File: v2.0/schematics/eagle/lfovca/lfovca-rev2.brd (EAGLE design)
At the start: 98.7 x 54.6 mm, 66 parts, among them IC1 TL082P, IC2 TL084P, T1 2N3904, T2 2N3904, T3 2N3904, T4 BC547, T5 BC547, T6 BC547

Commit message: LFOVCA: Optimize routes; cam outputs
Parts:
- moved R33 41.9 mm to (47.0, 39.4), turned to 270 degrees
- moved R13 38.1 mm to (69.8, 25.4), turned to 270 degrees
- moved R41 35.6 mm to (44.5, 12.7), turned to 0 degrees
- moved R39 25.5 mm to (31.8, 22.9), turned to 0 degrees
- moved R22 24.4 mm to (20.3, 11.4)
- moved R23 18.1 mm to (20.3, 15.2)
- moved R29 18.0 mm to (41.9, 22.9), turned to 0 degrees
- moved R34 17.8 mm to (49.5, 25.4)
- moved T2 14.2 mm to (5.08, 15.2)
- moved T3 14.2 mm to (11.4, 15.2)
- moved R8 12.6 mm to (81.3, 25.4), turned to 270 degrees
- moved R17 11.4 mm to (31.8, 11.4)
- moved R28 10.9 mm to (41.9, 26.7)
- moved R31 10.2 mm to (31.8, 26.7)
- moved R14 8.89 mm to (6.35, 24.1)
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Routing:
- net N$15: track 71.4 -> 13.8 mm, vias 2 -> 0
- net N$7: track 61.2 -> 25.8 mm, vias 1 -> 0
- net N$11: track 27.7 -> 9.05 mm
- net +12V: track 213.3 -> 198.5 mm, vias 0 -> 1
- net N$19: track 31.0 -> 16.5 mm
- net N$28: track 42.0 -> 27.9 mm, vias 1 -> 0
- net N$26: track 46.8 -> 32.8 mm
- net N$29: track 21.2 -> 7.93 mm
- net N$31: track 38.7 -> 51.8 mm, vias 1 -> 0
- net N$30: track 47.0 -> 58.7 mm
- net N$25: track 16.9 -> 7.34 mm
- net -12V: track 221.2 -> 230.2 mm, vias 1 -> 4
- net N$33: track 12.3 -> 20.6 mm
- net N$34: track 6.33 -> 14.4 mm
- net N$8: track 56.1 -> 50.0 mm, vias 1 -> 0
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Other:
- board text added: "ATTEN"
- board text added: "BIAS"
- board text added: "CV IN"
- board text added: "CV INIT"
- board text added: "LFO OUT"
- board text added: "LFOVCA rev2"
- board text added: "MIN LVL"
- board text added: "OFFSET"
- board text added: "RATE"
- board text added: "ROUND"
- board text added: "SYMM"

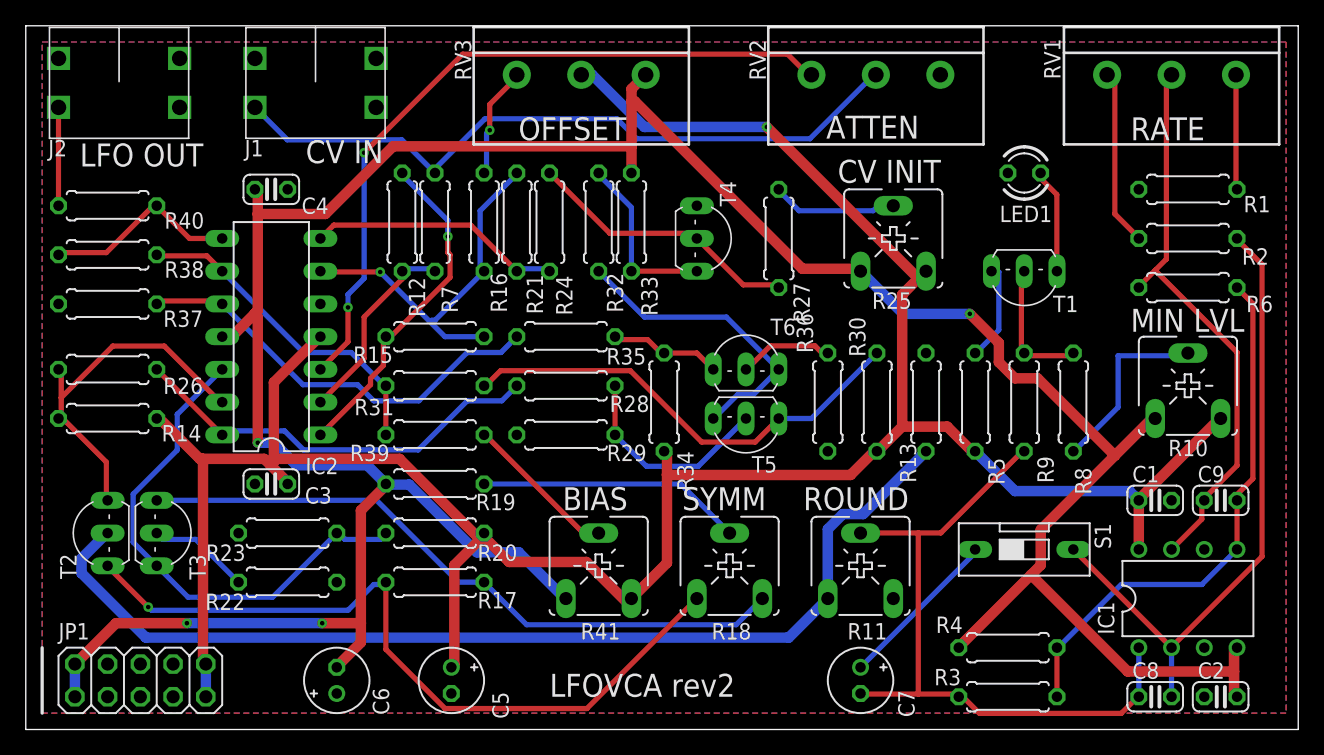
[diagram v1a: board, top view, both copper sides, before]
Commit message: LFOVCA board and panel revisions
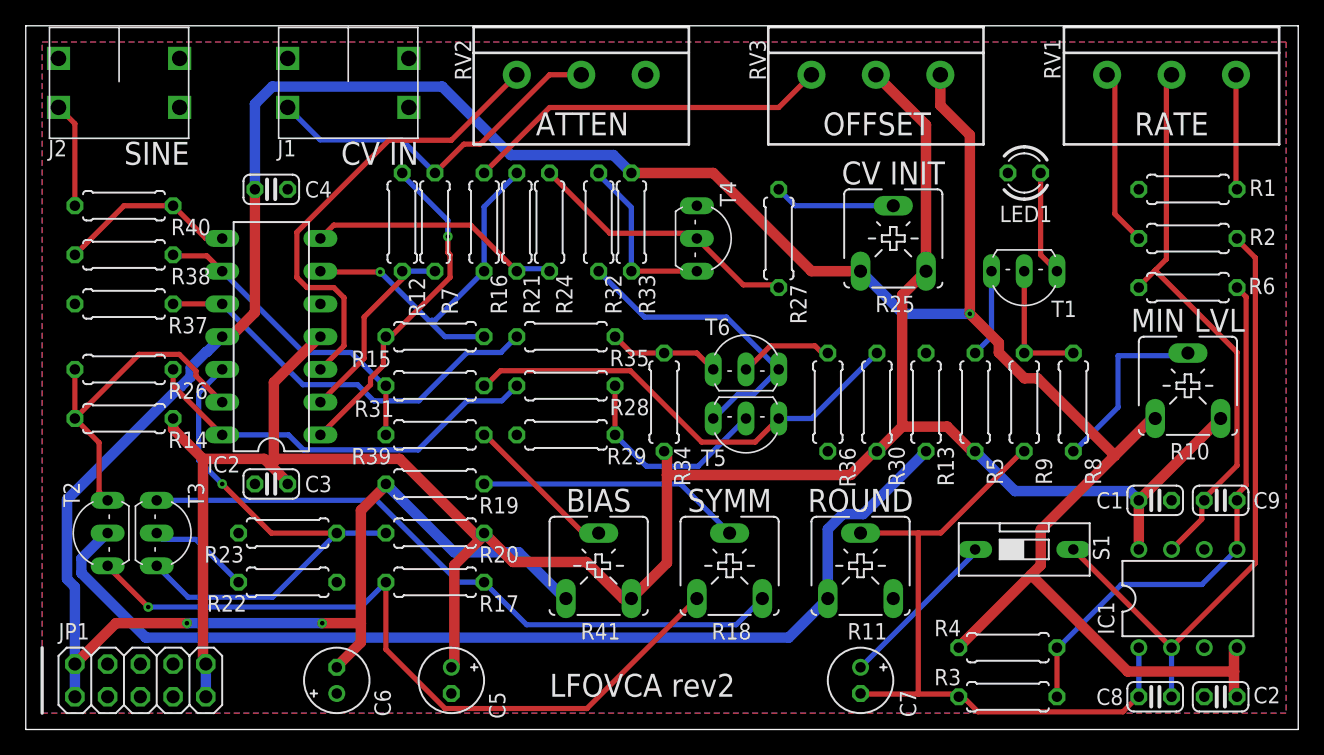
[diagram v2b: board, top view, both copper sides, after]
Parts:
- moved RV2 22.9 mm to (43.1, 50.8)
- moved RV3 22.9 mm to (66.0, 50.8)
- moved J1 2.54 mm to (20.3, 52.1)
- moved R14 1.27 mm to (7.62, 24.1)
- moved R26 1.27 mm to (7.62, 27.9)
- moved R37 1.27 mm to (7.62, 33.0)
- moved R38 1.27 mm to (7.62, 36.8)
- moved R40 1.27 mm to (7.62, 40.6)
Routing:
- net N$24: track 54.9 -> 28.0 mm
- net -12V: track 230.2 -> 255.9 mm, vias 4 -> 3
- net N$3: track 56.8 -> 36.3 mm, vias 2 -> 0
- net N$1: track 8.67 -> 28.6 mm, vias 1 -> 0
- net +12V: track 198.5 -> 181.3 mm, vias 1 -> 0
- net N$27: track 40.2 -> 41.7 mm, vias 0 -> 1
- net N$14: track 33.4 -> 31.8 mm
- net N$28: track 27.9 -> 26.5 mm
- net N$20: track 15.4 -> 14.1 mm
- net N$7: track 25.8 -> 24.5 mm
- net N$35: track 7.67 -> 6.88 mm
- net N$26: track 32.8 -> 32.1 mm
- net N$36: track 10.9 -> 10.2 mm
- net N$21: track 7.63 -> 8.16 mm
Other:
- board text added: "SINE"
- board text removed: "LFO OUT"

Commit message: Panel revisions; VCF-LP board layout
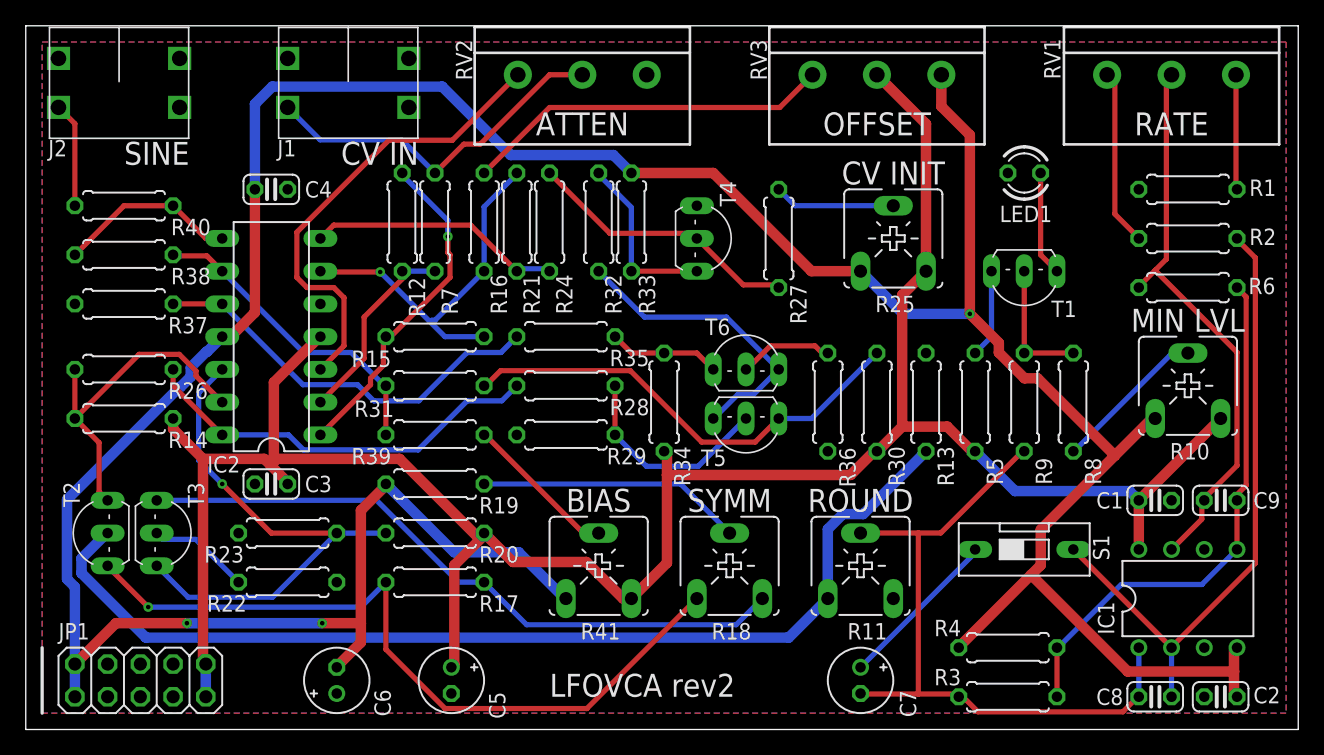
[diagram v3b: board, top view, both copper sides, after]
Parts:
- moved RV3 0.08 mm to (66.0, 50.8)
- moved RV2 0.08 mm to (43.2, 50.8)
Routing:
- net N$34: track 14.4 -> 12.0 mm
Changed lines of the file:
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@@
 <attribute name="VALUE" x="91.71" y="48.28" size="1.27" layer="27" rot="R180"/>
 </element>
-<element name="RV2" library="_common" package="_COMMON_3RP/1610N" value="250K (B)" x="43.1" y="50.8" smashed="yes" rot="R180">
-<attribute name="NAME" x="33.29" y="53.53" size="1.27" layer="25" rot="R270"/>
-<attribute name="VALUE" x="45.91" y="48.28" size="1.27" layer="27" rot="R180"/>
-</element>
-<element name="RV3" library="_common" package="_COMMON_3RP/1610N" value="250K (B)" x="65.96" y="50.8" smashed="yes" rot="R180">
-<attribute name="NAME" x="56.15" y="53.53" size="1.27" layer="25" rot="R270"/>
-<attribute name="VALUE" x="68.77" y="48.28" size="1.27" layer="27" rot="R180"/>
+<element name="RV2" library="_common" package="_COMMON_3RP/1610N" value="250K (B)" x="43.18" y="50.8" smashed="yes" rot="R180">
+<attribute name="NAME" x="33.37" y="53.53" size="1.27" layer="25" rot="R270"/>
+<attribute name="VALUE" x="45.99" y="48.28" size="1.27" layer="27" rot="R180"/>
+</element>
+<element name="RV3" library="_common" package="_COMMON_3RP/1610N" value="250K (B)" x="66.04" y="50.8" smashed="yes" rot="R180">
+<attribute name="NAME" x="56.23" y="53.53" size="1.27" layer="25" rot="R270"/>
+<attribute name="VALUE" x="68.85" y="48.28" size="1.27" layer="27" rot="R180"/>
 </element>
 <element name="S1" library="switch-dil" library_urn="urn:adsk.eagle:library:375" package="DS-01" package3d_urn="urn:adsk.eagle:package:27201/2" value="" x="77.47" y="13.97" smashed="yes" rot="R270">
@@
 <contactref element="R16" pad="1"/>
 <wire x1="40.64" y1="48.26" x2="35.56" y2="43.18" width="0.4064" layer="1"/>
-<wire x1="60.96" y1="50.8" x2="58.42" y2="48.26" width="0.4064" layer="1"/>
-<wire x1="58.42" y1="48.26" x2="40.64" y2="48.26" width="0.4064" layer="1"/>
+<wire x1="61.04" y1="50.8" x2="58.5" y2="48.26" width="0.4064" layer="1"/>
+<wire x1="58.5" y1="48.26" x2="40.64" y2="48.26" width="0.4064" layer="1"/>
 </signal>
 <signal name="+12V" class="1">
@@
 <wire x1="66.04" y1="21.59" x2="65.84" y2="21.59" width="0.8128" layer="1"/>
 <wire x1="65.84" y1="21.59" x2="64" y2="19.75" width="0.8128" layer="1"/>
-<wire x1="65.96" y1="50.8" x2="69.85" y2="46.91" width="0.8128" layer="1"/>
-<wire x1="69.85" y1="46.91" x2="69.85" y2="35.56" width="0.8128" layer="1"/>
 <wire x1="68" y1="23.5" x2="68" y2="33.71" width="0.8128" layer="1"/>
 <wire x1="68" y1="33.71" x2="69.85" y2="35.56" width="0.8128" layer="1"/>
@@
 <wire x1="43.5" y1="13" x2="37.8" y2="13" width="0.8128" layer="1"/>
 <wire x1="37.8" y1="13" x2="35.56" y2="15.24" width="0.8128" layer="1"/>
+<wire x1="66.04" y1="50.8" x2="69.85" y2="46.99" width="0.8128" layer="1"/>
+<wire x1="69.85" y1="46.99" x2="69.85" y2="35.56" width="0.8128" layer="1"/>
 </signal>
 <signal name="-12V" class="1">
@@
 <wire x1="93.98" y1="6.35" x2="93.75" y2="6.12" width="0.8128" layer="1"/>
 <wire x1="93.75" y1="6.12" x2="93.75" y2="4.5" width="0.8128" layer="1"/>
-<wire x1="70.96" y1="50.8" x2="70.96" y2="48.42" width="0.8128" layer="1"/>
 <wire x1="64.77" y1="35.56" x2="60.96" y2="35.56" width="0.8128" layer="1"/>
 <wire x1="53.34" y1="43.18" x2="46.99" y2="43.18" width="0.8128" layer="1"/>
@@
 <wire x1="27.94" y1="19.05" x2="33.24" y2="13.75" width="0.8128" layer="16"/>
 <wire x1="33.24" y1="13.75" x2="38.25" y2="13.75" width="0.8128" layer="16"/>
-<wire x1="70.96" y1="48.42" x2="73.25" y2="46.13" width="0.8128" layer="1"/>
 <wire x1="73.25" y1="46.13" x2="73.25" y2="32.25" width="0.8128" layer="1"/>
 <wire x1="26" y1="6.75" x2="24.13" y2="4.88" width="0.8128" layer="1"/>
@@
 <wire x1="19.1254125" y1="49.8812" x2="17.78" y2="48.5357875" width="0.8128" layer="16"/>
 <wire x1="17.78" y1="48.5357875" x2="17.78" y2="41.91" width="0.8128" layer="16"/>
+<wire x1="71.04" y1="50.8" x2="71.04" y2="48.34" width="0.8128" layer="1"/>
+<wire x1="71.04" y1="48.34" x2="73.25" y2="46.13" width="0.8128" layer="1"/>
 </signal>
 <signal name="N$6">
@@
 <contactref element="IC2" pad="3"/>
 <contactref element="RV2" pad="3"/>
-<wire x1="38.1" y1="50.8" x2="33.02" y2="45.72" width="0.4064" layer="1"/>
-<wire x1="33.02" y1="45.72" x2="28.16723125" y2="45.72" width="0.4064" layer="1"/>
 <wire x1="28.16723125" y1="45.72" x2="21.0312" y2="38.58396875" width="0.4064" layer="1"/>
 <wire x1="21.0312" y1="38.58396875" x2="21.0312" y2="35.07603125" width="0.4064" layer="1"/>
@@
 <wire x1="24.6888" y1="33.50396875" x2="24.6888" y2="29.7688" width="0.4064" layer="1"/>
 <wire x1="24.6888" y1="29.7688" x2="22.86" y2="27.94" width="0.4064" layer="1"/>
+<wire x1="38.18" y1="50.8" x2="33.1" y2="45.72" width="0.4064" layer="1"/>
+<wire x1="33.1" y1="45.72" x2="28.16723125" y2="45.72" width="0.4064" layer="1"/>
 </signal>
 <signal name="N$22">
@@
 <wire x1="33.985196875" y1="45.415196875" x2="31.75" y2="43.18" width="0.4064" layer="1"/>
 <wire x1="35.255196875" y1="45.415196875" x2="33.985196875" y2="45.415196875" width="0.4064" layer="1"/>
-<wire x1="43.1" y1="50.8" x2="40.64" y2="50.8" width="0.4064" layer="1"/>
+<wire x1="43.18" y1="50.8" x2="40.64" y2="50.8" width="0.4064" layer="1"/>
 <wire x1="40.64" y1="50.8" x2="35.255196875" y2="45.415196875" width="0.4064" layer="1"/>
 </signal>
@@
 <contactref element="R8" pad="2"/>
 <contactref element="R10" pad="S"/>
-<wire x1="84.75" y1="25" x2="81.5" y2="21.75" width="0.4064" layer="16"/>
-<wire x1="84.75" y1="29" x2="84.75" y2="25" width="0.4064" layer="16"/>
-<wire x1="90" y1="29" x2="84.75" y2="29" width="0.4064" layer="16"/>
-<wire x1="81.5" y1="21.75" x2="81.28" y2="21.59" width="0.4064" layer="16"/>
-<wire x1="90" y1="29" x2="90.17" y2="29.21" width="0.4064" layer="16"/>
+<wire x1="90.17" y1="29.21" x2="89.96" y2="29" width="0.4064" layer="16"/>
+<wire x1="81.34" y1="21.59" x2="81.28" y2="21.59" width="0.4064" layer="16"/>
+<wire x1="89.96" y1="29" x2="88.75" y2="29" width="0.4064" layer="16"/>
+<wire x1="88.75" y1="29" x2="81.34" y2="21.59" width="0.4064" layer="16"/>
 </signal>
 <signal name="N$21">
